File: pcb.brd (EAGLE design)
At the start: 117 x 137 mm, 22 parts, among them J3 POWER_JACKPTH_BREAD, U1 BOB-12009

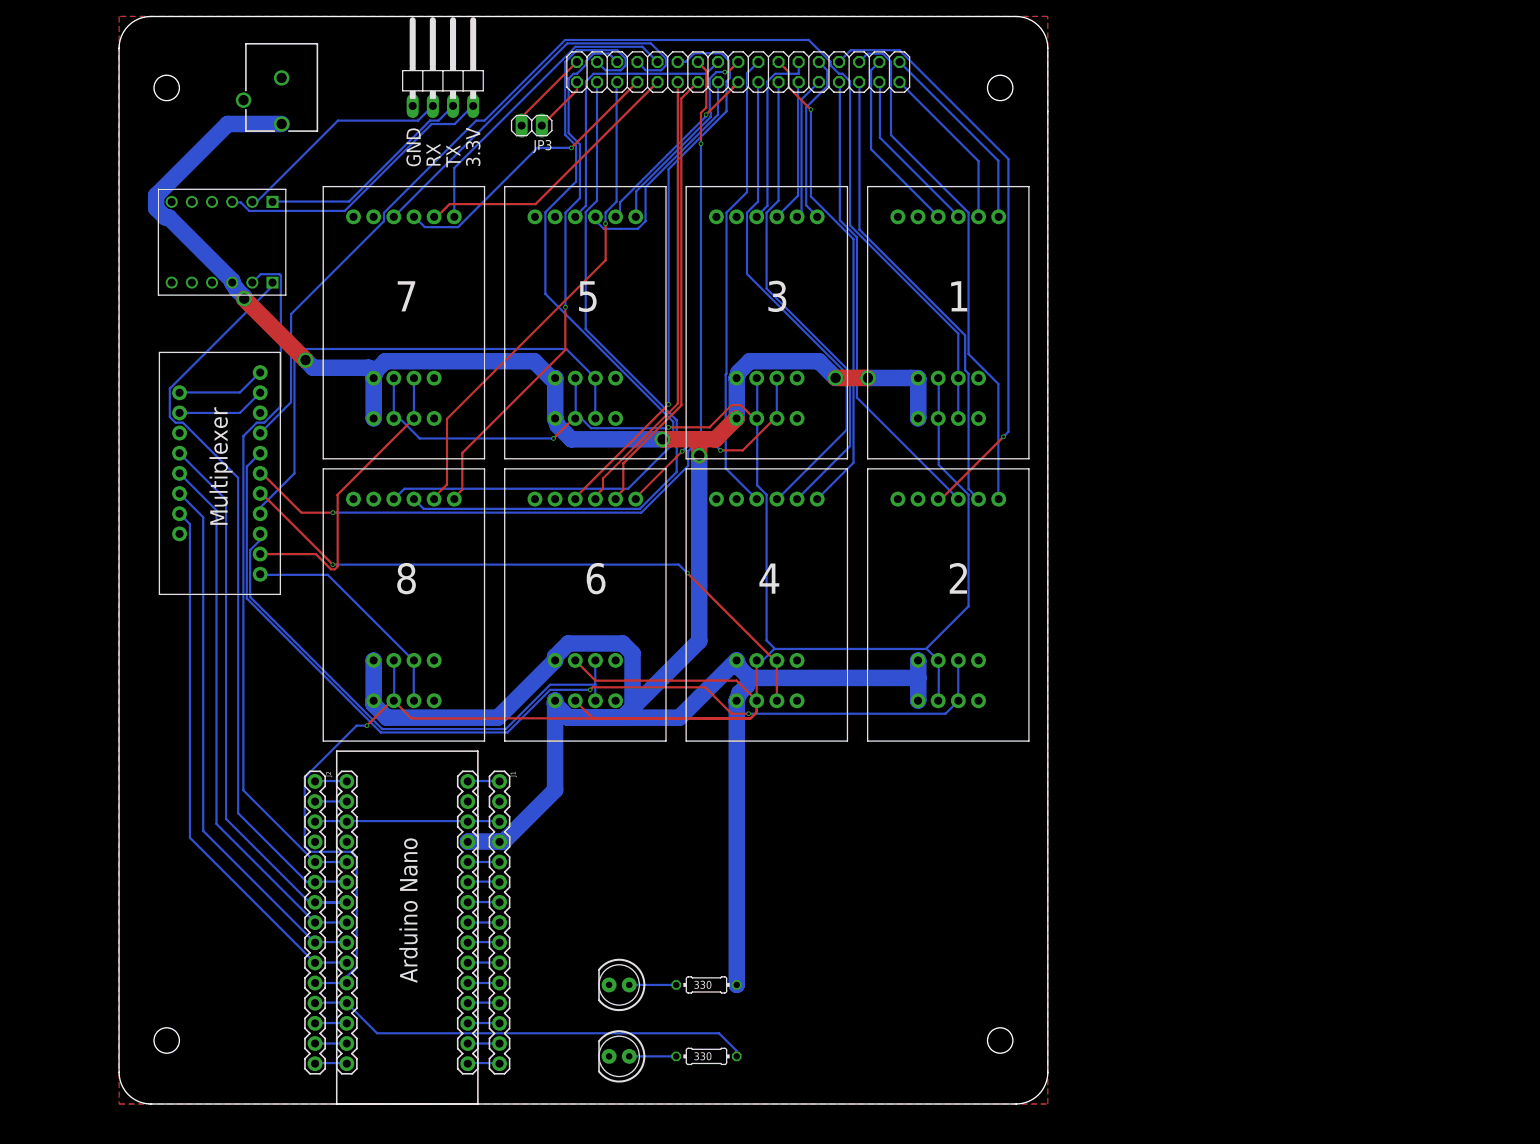
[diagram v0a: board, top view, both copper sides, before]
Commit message: Modified design so that it respects the height constraint
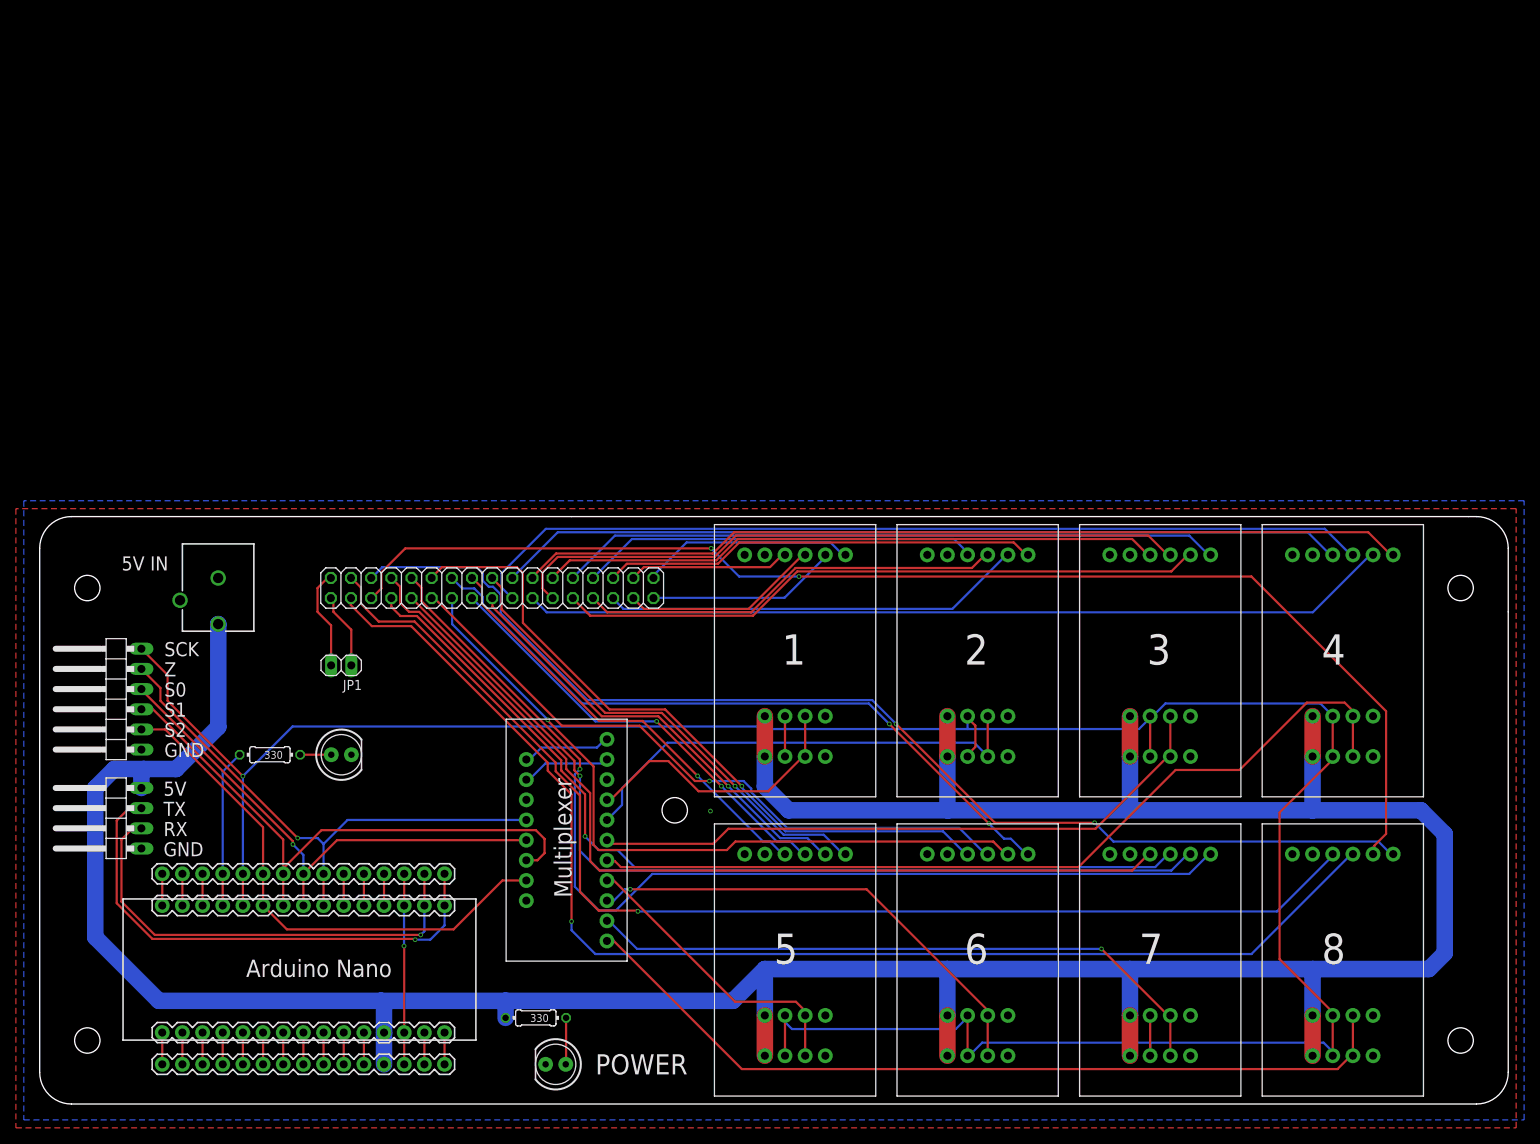
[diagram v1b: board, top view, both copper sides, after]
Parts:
- removed JP3: (no value), pinhead:1X02
- removed U1: BOB-12009, BOB-12009:CONV_BOB-12009
- added CONN_1: (no value), pinhead:2X17
- added JP4: (no value), pinhead:1X06/90
- JP1: device pinhead:2X17 -> pinhead:1X02
- moved 8 126.5 mm to (154.0, 1.00)
- moved 7 124.6 mm to (131.0, 1.00)
- moved JP2 102.5 mm to (9.00, 36.0), turned to 90 degrees
- moved JP1 89.9 mm to (38.0, 55.3)
- moved 5 84.5 mm to (85.0, 1.00)
- moved 4 72.9 mm to (154.0, 38.7)
- moved R2 66.9 mm to (29.0, 44.0), turned to 180 degrees
- moved 6 66.6 mm to (108.0, 1.00)
- moved 3 65.3 mm to (131.0, 38.7)
- moved U$10 63.6 mm to (74.0, 18.0)
- moved J3 63.5 mm to (22.5, 74.2)
- moved D3 51.7 mm to (38.0, 44.0), turned to 0 degrees
- moved 1 46.7 mm to (85.0, 38.7)
- moved J1 36.3 mm to (51.0, 5.00), turned to 180 degrees
- moved J51 31.8 mm to (51.0, 9.00), turned to 180 degrees
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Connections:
- removed net 3.3V: JP2.4, U1.LV
- removed net D4: J2.7, J52.7, U$10.5
- removed net D5: J2.8, J52.8, U$10.4
- removed net D6: J2.9, J52.9, U$10.3
- removed net D7: J2.10, J52.10, U$10.2
- removed net D8: 1.2, 1.2.2, 2.2, 2.2.2, 3.2, 3.2.2, 4.2, 4.2.2, 5.2, 5.2.2, 6.2, 6.2.2, 7.2, 7.2.2, 8.2, 8.2.2, J2.11, J52.11
- removed net RX: JP2.2, U1.LV2
- removed net TX: JP2.3, U1.LV1
- new net D4/Z: J2.7, J52.7, JP4.5, U$10.5
- new net D5/S0: J2.8, J52.8, JP4.4, U$10.4
- new net D6/S1: J2.9, J52.9, JP4.3, U$10.3
- new net D7/S2: J2.10, J52.10, JP4.2, U$10.2
- new net D8/HX711_SCK: 1.2, 1.2.2, 2.2, 2.2.2, 3.2, 3.2.2, 4.2, 4.2.2, 5.2, 5.2.2, 6.2, 6.2.2, 7.2, 7.2.2, 8.2, 8.2.2, J2.11, J52.11, JP4.6
- net 5.0V: now also JP2.4; no longer U1.HV
- net A+1: now also CONN_1.3; no longer JP1.3
- net A+2: now also CONN_1.7; no longer JP1.7
- net A+3: now also CONN_1.11; no longer JP1.11
- net A+4: now also CONN_1.15; no longer JP1.15
- net A+5: now also CONN_1.19; no longer JP1.19
- net A+6: now also CONN_1.23; no longer JP1.23
- net A+7: now also CONN_1.27; no longer JP1.27
- net A+8: now also CONN_1.31; no longer JP1.31
- net A-1: now also CONN_1.4; no longer JP1.4
- net A-2: now also CONN_1.8; no longer JP1.8
- net A-3: now also CONN_1.12; no longer JP1.12
- net A-4: now also CONN_1.16; no longer JP1.16
- net A-5: now also CONN_1.20; no longer JP1.20
- net A-6: now also CONN_1.24; no longer JP1.24
- net A-7: now also CONN_1.28; no longer JP1.28
- net A-8: now also CONN_1.32; no longer JP1.32
- net D2: no longer U1.HV2
- net D3: no longer U1.HV1
- net E+1: now also CONN_1.1; no longer JP1.1
- net E+2: now also CONN_1.5; no longer JP1.5
- net E+3: now also CONN_1.9; no longer JP1.9
- net E+4: now also CONN_1.13; no longer JP1.13
- net E+5: now also CONN_1.17; no longer JP1.17
- net E+6: now also CONN_1.21; no longer JP1.21
- net E+7: now also CONN_1.25; no longer JP1.25
- net E+8: now also CONN_1.29; no longer JP1.29
- net E-1: now also CONN_1.2; no longer JP1.2
- net E-2: now also CONN_1.6; no longer JP1.6
- net E-3: now also CONN_1.10; no longer JP1.10
- net E-4: now also CONN_1.14; no longer JP1.14
- net E-5: now also CONN_1.18; no longer JP1.18
- net E-6: now also CONN_1.22; no longer JP1.22
- net E-7: now also CONN_1.26; no longer JP1.26
- net E-8: now also CONN_1.30; no longer JP1.30
- net GND: now also JP4.1; no longer U1.GND_1, U1.GND_2
- net P1: now also CONN_1.34, JP1.1; no longer JP1.34, JP3.1
- net P2: now also CONN_1.33, JP1.2; no longer JP1.33, JP3.2
- net RX0: now also JP2.2
- net TX1: now also JP2.3
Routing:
- net D8/HX711_SCK: track 0.00 -> 337.0 mm, vias 0 -> 1
- net D8: track 323.1 -> 0.00 mm, vias 3 -> 0
- net DT1: track 152.5 -> 35.6 mm
- net E-8: track 62.1 -> 158.8 mm, vias 1 -> 2
- net E+7: track 38.9 -> 132.3 mm, vias 0 -> 1
- net D3: track 93.7 -> 4.00 mm
- net D2: track 88.2 -> 4.00 mm
- net E-7: track 35.2 -> 119.4 mm, vias 0 -> 1
- net A-7: track 36.2 -> 117.3 mm
- net E+8: track 68.3 -> 146.2 mm, vias 1 -> 2
- net DT8: track 29.0 -> 106.6 mm
- net D6/S1: track 0.00 -> 72.8 mm
- net D4: track 72.1 -> 0.00 mm
- net A-8: track 90.0 -> 161.2 mm, vias 0 -> 1
- net A+7: track 49.3 -> 118.7 mm
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- added copper zone on layer 16, net GND
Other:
- board size 117 x 137 mm -> 185 x 74 mm
- board text added: "5V"
- board text added: "5V IN"
- board text added: "POWER"
- board text added: "S0"
- board text added: "S1"
- board text added: "S2"
- board text added: "SCK"
- board text added: "Z"
- board text removed: "3.3V"
